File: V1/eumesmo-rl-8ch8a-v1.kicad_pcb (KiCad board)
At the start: 2 copper layers, 98 x 67.8 mm, 48 parts, among them J1 250-202, J2 250-204, J3 250-204, J4 DB142V-5.08-4P, J5 DB142V-5.08-4P, J6 DB142V-5.08-4P, J7 DB142V-5.08-4P, K1 G5Q-1A4-DC24V, K2 G5Q-1A4-DC24V, K3 G5Q-1A4-DC24V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

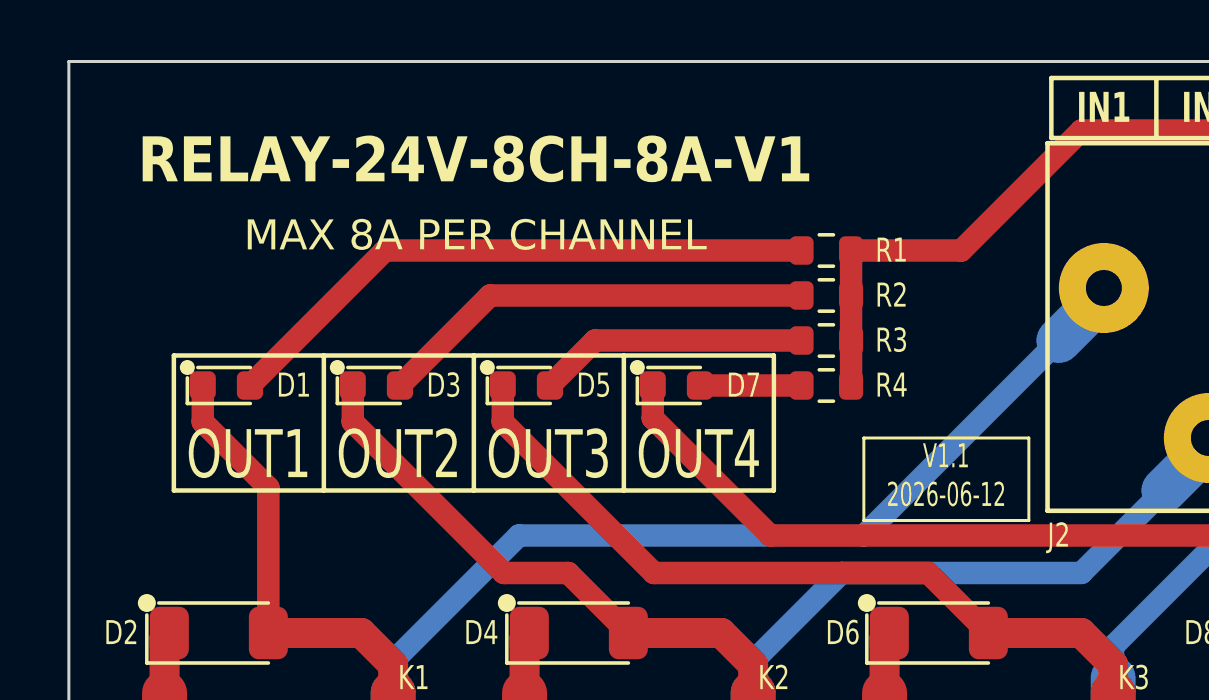
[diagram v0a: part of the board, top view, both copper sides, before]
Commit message: Renamed files to align with eumesmo branding.
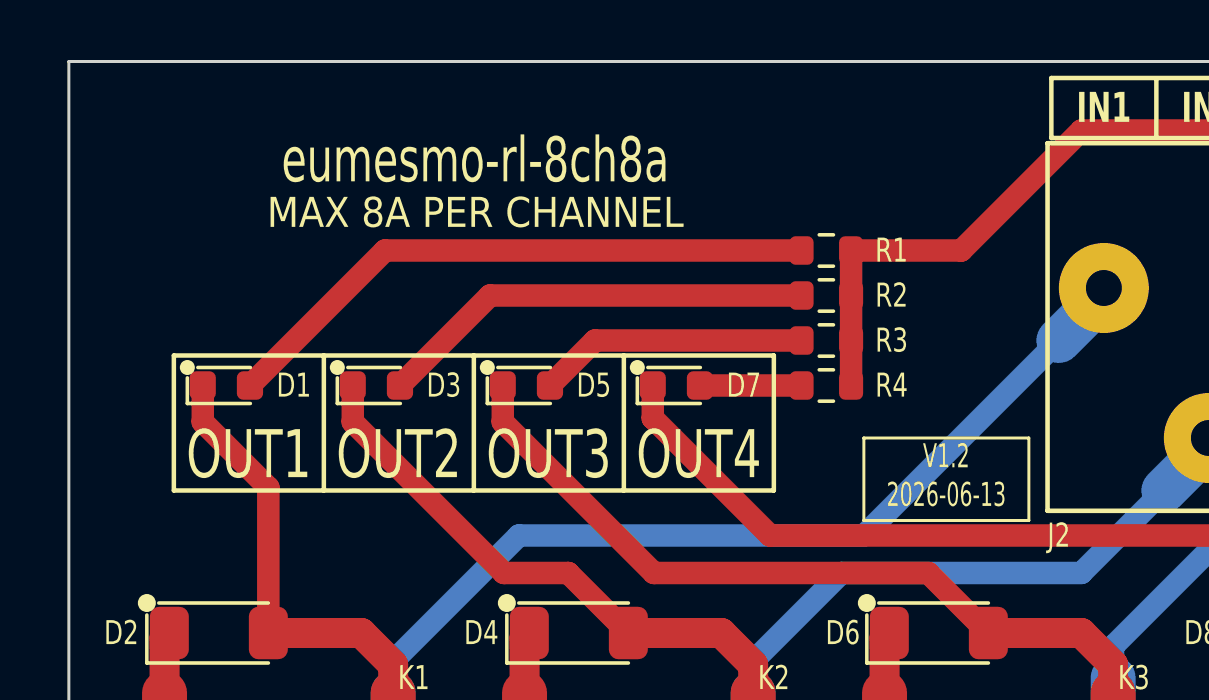
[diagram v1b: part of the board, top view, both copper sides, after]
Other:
- board text added: "V1.2 2026-06-13"
- board text added: "eumesmo-rl-8ch8a"
- board text removed: "RELAY-24V-8CH-8A-V1"
- board text removed: "V1.1 2026-06-12"
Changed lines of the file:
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@@
 	(paper "A4")
 	(title_block
-		(title "ESP 8 Relay Module")
-		(date "2026-06-12")
-		(rev "V1.1")
+		(title "eumesmo 8x 24V 8A NO Relay Module")
+		(date "2026-06-13")
+		(rev "V1.2")
 	)
 	(layers
@@
 		(property ki_fp_filters "TO-???* *_Diode_* *SingleDiode* D_*")
 		(sheetname "/")
-		(sheetfile "relay-24v-8ch-8a-v1.kicad_sch")
+		(sheetfile "eumesmo-rl-8ch8a-v1.kicad_sch")
 		(units
 			(unit
@@
 		(property ki_fp_filters "TO-???* *_Diode_* *SingleDiode* D_*")
 		(sheetname "/")
-		(sheetfile "relay-24v-8ch-8a-v1.kicad_sch")
+		(sheetfile "eumesmo-rl-8ch8a-v1.kicad_sch")
 		(units
 			(unit
@@
 		(property ki_fp_filters "LED* LED_SMD:* LED_THT:*")
 		(sheetname "/")
-		(sheetfile "relay-24v-8ch-8a-v1.kicad_sch")
+		(sheetfile "eumesmo-rl-8ch8a-v1.kicad_sch")
 		(units
 			(unit
@@
 		(property ki_fp_filters "R_*")
 		(sheetname "/")
-		(sheetfile "relay-24v-8ch-8a-v1.kicad_sch")
+		(sheetfile "eumesmo-rl-8ch8a-v1.kicad_sch")
 		(units
 			(unit
@@
 		(property ki_fp_filters "R_*")
 		(sheetname "/")
-		(sheetfile "relay-24v-8ch-8a-v1.kicad_sch")
+		(sheetfile "eumesmo-rl-8ch8a-v1.kicad_sch")
 		(units
 			(unit
@@
 		(property ki_fp_filters "LED* LED_SMD:* LED_THT:*")
 		(sheetname "/")
-		(sheetfile "relay-24v-8ch-8a-v1.kicad_sch")
+		(sheetfile "eumesmo-rl-8ch8a-v1.kicad_sch")
 		(units
 			(unit
@@
 		(property ki_fp_filters "TO-???* *_Diode_* *SingleDiode* D_*")
 		(sheetname "/")
-		(sheetfile "relay-24v-8ch-8a-v1.kicad_sch")
+		(sheetfile "eumesmo-rl-8ch8a-v1.kicad_sch")
 		(units
 			(unit
@@
 		(property ki_fp_filters "R_*")
 		(sheetname "/")
-		(sheetfile "relay-24v-8ch-8a-v1.kicad_sch")
+		(sheetfile "eumesmo-rl-8ch8a-v1.kicad_sch")
 		(units
 			(unit
@@
 		(property ki_fp_filters "LED* LED_SMD:* LED_THT:*")
 		(sheetname "/")
-		(sheetfile "relay-24v-8ch-8a-v1.kicad_sch")
+		(sheetfile "eumesmo-rl-8ch8a-v1.kicad_sch")
 		(units
 			(unit
@@
 		(property ki_fp_filters "Relay*SPST*Omron*G5PZ*")
 		(sheetname "/")
-		(sheetfile "relay-24v-8ch-8a-v1.kicad_sch")
+		(sheetfile "eumesmo-rl-8ch8a-v1.kicad_sch")
 		(units
 			(unit
@@
 		(property ki_fp_filters "LED* LED_SMD:* LED_THT:*")
 		(sheetname "/")
-		(sheetfile "relay-24v-8ch-8a-v1.kicad_sch")
+		(sheetfile "eumesmo-rl-8ch8a-v1.kicad_sch")
 		(units
 			(unit
@@
 		(property ki_fp_filters "Relay*SPST*Omron*G5PZ*")
 		(sheetname "/")
-		(sheetfile "relay-24v-8ch-8a-v1.kicad_sch")
+		(sheetfile "eumesmo-rl-8ch8a-v1.kicad_sch")
 		(units
 			(unit
@@
 		(property ki_fp_filters "R_*")
 		(sheetname "/")
-		(sheetfile "relay-24v-8ch-8a-v1.kicad_sch")
+		(sheetfile "eumesmo-rl-8ch8a-v1.kicad_sch")
 		(units
 			(unit
@@
 		(property ki_fp_filters "R_*")
 		(sheetname "/")
-		(sheetfile "relay-24v-8ch-8a-v1.kicad_sch")
+		(sheetfile "eumesmo-rl-8ch8a-v1.kicad_sch")
 		(units
 			(unit
@@
 		(property ki_fp_filters "Relay*SPST*Omron*G5PZ*")
 		(sheetname "/")
-		(sheetfile "relay-24v-8ch-8a-v1.kicad_sch")
+		(sheetfile "eumesmo-rl-8ch8a-v1.kicad_sch")
 		(units
 			(unit
@@
 		(property ki_fp_filters "LED* LED_SMD:* LED_THT:*")
 		(sheetname "/")
-		(sheetfile "relay-24v-8ch-8a-v1.kicad_sch")
+		(sheetfile "eumesmo-rl-8ch8a-v1.kicad_sch")
 		(units
 			(unit
@@
 		(property ki_fp_filters "R_*")
 		(sheetname "/")
-		(sheetfile "relay-24v-8ch-8a-v1.kicad_sch")
+		(sheetfile "eumesmo-rl-8ch8a-v1.kicad_sch")
 		(units
 			(unit
@@
 		(property ki_fp_filters "TO-???* *_Diode_* *SingleDiode* D_*")
 		(sheetname "/")
-		(sheetfile "relay-24v-8ch-8a-v1.kicad_sch")
+		(sheetfile "eumesmo-rl-8ch8a-v1.kicad_sch")
 		(units
 			(unit
@@
 		(property ki_fp_filters "Connector*:*_1x??_*")
 		(sheetname "/")
-		(sheetfile "relay-24v-8ch-8a-v1.kicad_sch")
+		(sheetfile "eumesmo-rl-8ch8a-v1.kicad_sch")
 		(units
 			(unit
@@
 		(property ki_fp_filters "RV_* Varistor*")
 		(sheetname "/")
-		(sheetfile "relay-24v-8ch-8a-v1.kicad_sch")
+		(sheetfile "eumesmo-rl-8ch8a-v1.kicad_sch")
 		(units
 			(unit
@@
 		(property ki_fp_filters "LED* LED_SMD:* LED_THT:*")
 		(sheetname "/")
-		(sheetfile "relay-24v-8ch-8a-v1.kicad_sch")
+		(sheetfile "eumesmo-rl-8ch8a-v1.kicad_sch")
 		(units
 			(unit
@@
 		(property ki_fp_filters "TO-???* *_Diode_* *SingleDiode* D_*")
 		(sheetname "/")
-		(sheetfile "relay-24v-8ch-8a-v1.kicad_sch")
+		(sheetfile "eumesmo-rl-8ch8a-v1.kicad_sch")
 		(units
 			(unit
@@
 		(property ki_fp_filters "Connector*:*_1x??_*")
 		(sheetname "/")
-		(sheetfile "relay-24v-8ch-8a-v1.kicad_sch")
+		(sheetfile "eumesmo-rl-8ch8a-v1.kicad_sch")
 		(units
 			(unit
@@
 		(property ki_fp_filters "RV_* Varistor*")
 		(sheetname "/")
-		(sheetfile "relay-24v-8ch-8a-v1.kicad_sch")
+		(sheetfile "eumesmo-rl-8ch8a-v1.kicad_sch")
 		(units
 			(unit
@@
 		(property ki_fp_filters "Connector*:*_1x??_*")
 		(sheetname "/")
-		(sheetfile "relay-24v-8ch-8a-v1.kicad_sch")
+		(sheetfile "eumesmo-rl-8ch8a-v1.kicad_sch")
 		(units
 			(unit
@@
 		(property ki_fp_filters "R_*")
 		(sheetname "/")
-		(sheetfile "relay-24v-8ch-8a-v1.kicad_sch")
+		(sheetfile "eumesmo-rl-8ch8a-v1.kicad_sch")
 		(units
 			(unit
@@
 		(property ki_fp_filters "Connector*:*_1x??_*")
 		(sheetname "/")
-		(sheetfile "relay-24v-8ch-8a-v1.kicad_sch")
+		(sheetfile "eumesmo-rl-8ch8a-v1.kicad_sch")
 		(units
 			(unit
@@
 		(property ki_fp_filters "RV_* Varistor*")
 		(sheetname "/")
-		(sheetfile "relay-24v-8ch-8a-v1.kicad_sch")
+		(sheetfile "eumesmo-rl-8ch8a-v1.kicad_sch")
 		(units
 			(unit
@@
 		(property ki_fp_filters "LED* LED_SMD:* LED_THT:*")
 		(sheetname "/")
-		(sheetfile "relay-24v-8ch-8a-v1.kicad_sch")
+		(sheetfile "eumesmo-rl-8ch8a-v1.kicad_sch")
 		(units
 			(unit
@@
 		(property ki_fp_filters "RV_* Varistor*")
 		(sheetname "/")
-		(sheetfile "relay-24v-8ch-8a-v1.kicad_sch")
+		(sheetfile "eumesmo-rl-8ch8a-v1.kicad_sch")
 		(units
 			(unit
@@
 		(property ki_fp_filters "RV_* Varistor*")
 		(sheetname "/")
-		(sheetfile "relay-24v-8ch-8a-v1.kicad_sch")
+		(sheetfile "eumesmo-rl-8ch8a-v1.kicad_sch")
 		(units
 			(unit
@@
 		(property ki_fp_filters "RV_* Varistor*")
 		(sheetname "/")
-		(sheetfile "relay-24v-8ch-8a-v1.kicad_sch")
+		(sheetfile "eumesmo-rl-8ch8a-v1.kicad_sch")
 		(units
 			(unit
@@
 		(property ki_fp_filters "Relay*SPST*Omron*G5PZ*")
 		(sheetname "/")
-		(sheetfile "relay-24v-8ch-8a-v1.kicad_sch")
+		(sheetfile "eumesmo-rl-8ch8a-v1.kicad_sch")
 		(units
 			(unit
@@
 		(property ki_fp_filters "TO-???* *_Diode_* *SingleDiode* D_*")
 		(sheetname "/")
-		(sheetfile "relay-24v-8ch-8a-v1.kicad_sch")
+		(sheetfile "eumesmo-rl-8ch8a-v1.kicad_sch")
 		(units
 			(unit
@@
 		(property ki_fp_filters "TO-???* *_Diode_* *SingleDiode* D_*")
 		(sheetname "/")
-		(sheetfile "relay-24v-8ch-8a-v1.kicad_sch")
+		(sheetfile "eumesmo-rl-8ch8a-v1.kicad_sch")
 		(units
 			(unit
@@
 		(property ki_fp_filters "Relay*SPST*Omron*G5PZ*")
 		(sheetname "/")
-		(sheetfile "relay-24v-8ch-8a-v1.kicad_sch")
+		(sheetfile "eumesmo-rl-8ch8a-v1.kicad_sch")
 		(units
 			(unit
@@
 		(property ki_fp_filters "Relay*SPST*Omron*G5PZ*")
 		(sheetname "/")
-		(sheetfile "relay-24v-8ch-8a-v1.kicad_sch")
+		(sheetfile "eumesmo-rl-8ch8a-v1.kicad_sch")
 		(units
 			(unit
@@
 		(property ki_fp_filters "TO-???* *_Diode_* *SingleDiode* D_*")
 		(sheetname "/")
-		(sheetfile "relay-24v-8ch-8a-v1.kicad_sch")
+		(sheetfile "eumesmo-rl-8ch8a-v1.kicad_sch")
 		(units
 			(unit
@@
 		(property ki_fp_filters "Connector*:*_1x??_*")
 		(sheetname "/")
-		(sheetfile "relay-24v-8ch-8a-v1.kicad_sch")
+		(sheetfile "eumesmo-rl-8ch8a-v1.kicad_sch")
 		(units
 			(unit
@@
 		(property ki_fp_filters "Connector*:*_1x??_*")
 		(sheetname "/")
-		(sheetfile "relay-24v-8ch-8a-v1.kicad_sch")
+		(sheetfile "eumesmo-rl-8ch8a-v1.kicad_sch")
 		(units
 			(unit
@@
 		(property ki_fp_filters "RV_* Varistor*")
 		(sheetname "/")
-		(sheetfile "relay-24v-8ch-8a-v1.kicad_sch")
+		(sheetfile "eumesmo-rl-8ch8a-v1.kicad_sch")
 		(units
 			(unit
@@
 		(property ki_fp_filters "Relay*SPST*Omron*G5PZ*")
 		(sheetname "/")
-		(sheetfile "relay-24v-8ch-8a-v1.kicad_sch")
+		(sheetfile "eumesmo-rl-8ch8a-v1.kicad_sch")
 		(units
 			(unit
@@
 		(property ki_fp_filters "R_*")
 		(sheetname "/")
-		(sheetfile "relay-24v-8ch-8a-v1.kicad_sch")
+		(sheetfile "eumesmo-rl-8ch8a-v1.kicad_sch")
 		(units
 			(unit
@@
 		(property ki_fp_filters "LED* LED_SMD:* LED_THT:*")
 		(sheetname "/")
-		(sheetfile "relay-24v-8ch-8a-v1.kicad_sch")
+		(sheetfile "eumesmo-rl-8ch8a-v1.kicad_sch")
 		(units
 			(unit
@@
 		(property ki_fp_filters "Connector*:*_1x??_*")
 		(sheetname "/")
-		(sheetfile "relay-24v-8ch-8a-v1.kicad_sch")
+		(sheetfile "eumesmo-rl-8ch8a-v1.kicad_sch")
 		(units
 			(unit
@@
 		(property ki_fp_filters "Relay*SPST*Omron*G5PZ*")
 		(sheetname "/")
-		(sheetfile "relay-24v-8ch-8a-v1.kicad_sch")
+		(sheetfile "eumesmo-rl-8ch8a-v1.kicad_sch")
 		(units
 			(unit
@@
 		(property ki_fp_filters "RV_* Varistor*")
 		(sheetname "/")
-		(sheetfile "relay-24v-8ch-8a-v1.kicad_sch")
+		(sheetfile "eumesmo-rl-8ch8a-v1.kicad_sch")
 		(units
 			(unit
@@
 		(layer "Edge.Cuts")
 	)
-	(gr_text "V1.1\n2026-06-12"
+	(gr_text "V1.2\n2026-06-13"
 		(at 154.25 76 0)
 		(layer "F.SilkS")
@@
 	)
 	(gr_text "MAX 8A PER CHANNEL"
-		(at 138.55 68 0)
+		(at 138.55 67.25 0)
 		(layer "F.SilkS")
 		(effects
 			(font
-				(size 1 1)
+				(size 1 0.9)
 				(thickness 0.15)
 			)
@@
 		)
 	)
+	(gr_text "eumesmo-rl-8ch8a"
+		(at 138.55 65.5 0)
+		(layer "F.SilkS")
+		(effects
+			(font
+				(size 1.5 1)
+				(thickness 0.2)
+			)
+		)
+	)
 	(gr_text "OUT1"
 		(at 131 76.25 0)
@@
 		)
 	)
-	(gr_text "RELAY-24V-8CH-8A-V1"
-		(at 138.55 65.5 0)
-		(layer "F.SilkS")
-		(effects
-			(font
-				(size 1.5 1.3)
-				(thickness 0.25)
-				(bold yes)
-			)
-		)
-	)
